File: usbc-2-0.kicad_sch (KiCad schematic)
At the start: 7 parts

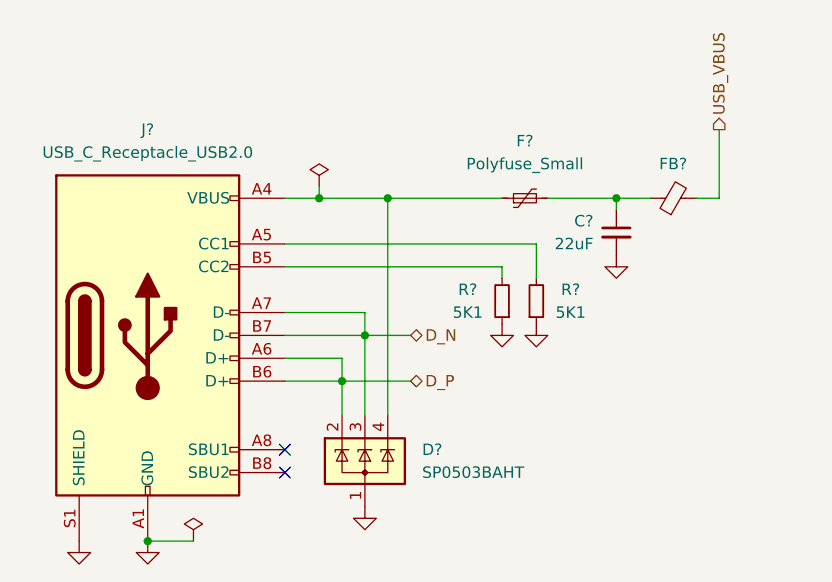
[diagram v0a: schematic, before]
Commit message: updated caps and power regulator
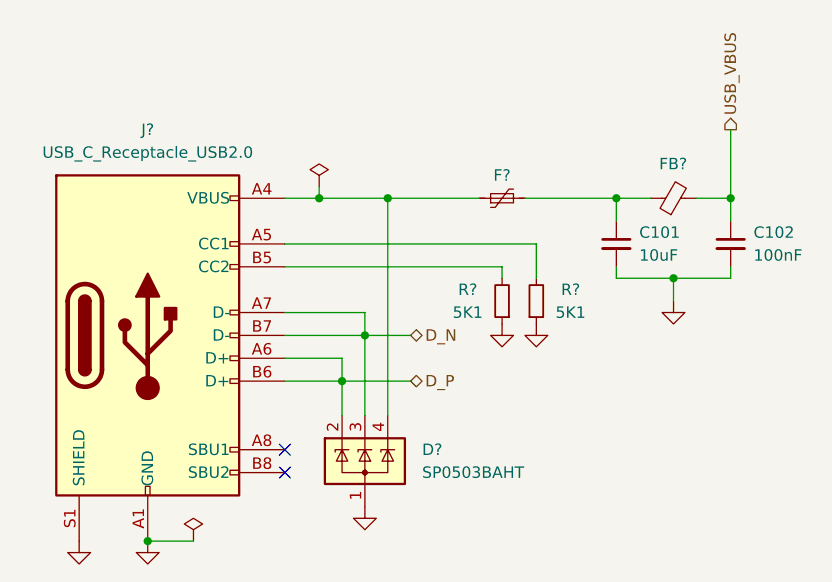
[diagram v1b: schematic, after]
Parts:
- removed C?: 22uF, Capacitor_SMD:C_0805_2012Metric, symbol Device:C_Small
- added C101: 10uF, Capacitor_SMD:C_0805_2012Metric, symbol Device:C_Small
- added C102: 100nF, Capacitor_SMD:C_0603_1608Metric, symbol Device:C_Small
- D?: LCSC (none) -> C7074
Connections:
- net GND: now also C101.2, C102.2
- net USB_VBUS: now also C102.1
- net at F?.2, FB?.1: now also C101.1
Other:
- moved on the sheet: F?
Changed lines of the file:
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@@
 (kicad_sch (version 20230121) (generator eeschema)
   (paper "A5")
+  (junction (at 109.22 46.99) (diameter 0) (color 0 0 0 0)
+  )
   (junction (at 74.93 53.34) (diameter 0) (color 0 0 0 0)
   )
@@
   )
   (junction (at 77.47 38.1) (diameter 0) (color 0 0 0 0)
+  )
+  (junction (at 115.57 38.1) (diameter 0) (color 0 0 0 0)
   )
   (junction (at 50.8 76.2) (diameter 0) (color 0 0 0 0)
@@
     (stroke (width 0) (type default))
   )
-  (wire (pts (xy 114.3 30.48) (xy 114.3 38.1))
+  (wire (pts (xy 115.57 30.48) (xy 115.57 38.1))
     (stroke (width 0) (type default))
   )
@@
     (stroke (width 0) (type default))
   )
+  (wire (pts (xy 115.57 46.99) (xy 115.57 45.72))
+    (stroke (width 0) (type default))
+  )
+  (wire (pts (xy 109.22 46.99) (xy 115.57 46.99))
+    (stroke (width 0) (type default))
+  )
   (wire (pts (xy 74.93 53.34) (xy 74.93 62.23))
     (stroke (width 0) (type default))
   )
-  (wire (pts (xy 102.87 39.37) (xy 102.87 38.1))
+  (wire (pts (xy 102.87 40.64) (xy 102.87 38.1))
     (stroke (width 0) (type default))
   )
@@
     (stroke (width 0) (type default))
   )
+  (wire (pts (xy 109.22 46.99) (xy 102.87 46.99))
+    (stroke (width 0) (type default))
+  )
   (wire (pts (xy 74.93 50.8) (xy 74.93 53.34))
     (stroke (width 0) (type default))
@@
     (stroke (width 0) (type default))
   )
-  (wire (pts (xy 77.47 38.1) (xy 90.17 38.1))
-    (stroke (width 0) (type default))
-  )
-  (wire (pts (xy 114.3 38.1) (xy 111.76 38.1))
+  (wire (pts (xy 77.47 38.1) (xy 87.63 38.1))
+    (stroke (width 0) (type default))
+  )
+  (wire (pts (xy 115.57 38.1) (xy 111.76 38.1))
+    (stroke (width 0) (type default))
+  )
+  (wire (pts (xy 115.57 38.1) (xy 115.57 40.64))
     (stroke (width 0) (type default))
   )
@@
     (stroke (width 0) (type default))
   )
+  (wire (pts (xy 102.87 46.99) (xy 102.87 45.72))
+    (stroke (width 0) (type default))
+  )
   (wire (pts (xy 50.8 76.2) (xy 55.88 76.2))
     (stroke (width 0) (type default))
@@
     (stroke (width 0) (type default))
   )
+  (wire (pts (xy 109.22 49.53) (xy 109.22 46.99))
+    (stroke (width 0) (type default))
+  )
   (wire (pts (xy 66.04 45.72) (xy 90.17 45.72))
     (stroke (width 0) (type default))
   )
-  (wire (pts (xy 95.25 38.1) (xy 102.87 38.1))
+  (wire (pts (xy 92.71 38.1) (xy 102.87 38.1))
     (stroke (width 0) (type default))
   )
@@
     (effects (font (size 1.27 1.27)) (justify left))
   )
-  (hierarchical_label "USB_VBUS" (shape output) (at 114.3 30.48 90) (fields_autoplaced)
+  (hierarchical_label "USB_VBUS" (shape output) (at 115.57 30.48 90) (fields_autoplaced)
     (effects (font (size 1.27 1.27)) (justify left))
   )
@@
     )
     (property "Datasheet" "http://www.littelfuse.com/~/media/files/littelfuse/technical%20resources/documents/data%20sheets/sp05xxba.pdf" (at 78.105 64.135 0)
+      (effects (font (size 1.27 1.27)) hide)
+    )
+    (property "LCSC" "C7074" (at 74.93 67.31 0)
       (effects (font (size 1.27 1.27)) hide)
     )
@@
     )
   )
+  (symbol (lib_id "Device:C_Small") (at 115.57 43.18 0) (unit 1)
+    (in_bom yes) (on_board yes) (dnp no)
+    (property "Reference" "C102" (at 118.11 41.91 0)
+      (effects (font (size 1.27 1.27)) (justify left))
+    )
+    (property "Value" "100nF" (at 118.11 44.45 0)
+      (effects (font (size 1.27 1.27)) (justify left))
+    )
+    (property "Footprint" "Capacitor_SMD:C_0603_1608Metric" (at 115.57 43.18 0)
+      (effects (font (size 1.27 1.27)) hide)
+    )
+    (property "Datasheet" "~" (at 115.57 43.18 0)
+      (effects (font (size 1.27 1.27)) hide)
+    )
+    (property "LCSC" "C14663" (at 115.57 43.18 0)
+      (effects (font (size 1.27 1.27)) hide)
+    )
+    (pin "1")
+    (pin "2")
+    (instances
+      (project "arudino-clone"
+        (path "/7b2b1845-59f7-4bfa-9efc-3639d821cf70"
+          (reference "C102") (unit 1)
+        )
+        (path "/7b2b1845-59f7-4bfa-9efc-3639d821cf70/42f81444-0f87-48cc-869b-f9c5fa4e11c4"
+          (reference "C202") (unit 1)
+        )
+      )
+    )
+  )
   (symbol (lib_id "Device:FerriteBead_Small") (at 109.22 38.1 90) (unit 1)
     (in_bom yes) (on_board yes) (dnp no) (fields_autoplaced)
@@
     )
   )
-  (symbol (lib_id "Device:Polyfuse_Small") (at 92.71 38.1 90) (unit 1)
-    (in_bom yes) (on_board yes) (dnp no) (fields_autoplaced)
-    (property "Reference" "F?" (at 92.71 31.75 90)
-      (effects (font (size 1.27 1.27)))
-    )
-    (property "Value" "Polyfuse_Small" (at 92.71 34.29 90)
-      (effects (font (size 1.27 1.27)))
-    )
-    (property "Footprint" "Fuse:Fuse_0603_1608Metric" (at 97.79 36.83 0)
+  (symbol (lib_id "Device:C_Small") (at 102.87 43.18 0) (unit 1)
+    (in_bom yes) (on_board yes) (dnp no)
+    (property "Reference" "C101" (at 105.41 41.91 0)
+      (effects (font (size 1.27 1.27)) (justify left))
+    )
+    (property "Value" "10uF" (at 105.41 44.45 0)
+      (effects (font (size 1.27 1.27)) (justify left))
+    )
+    (property "Footprint" "Capacitor_SMD:C_0805_2012Metric" (at 102.87 43.18 0)
+      (effects (font (size 1.27 1.27)) hide)
+    )
+    (property "Datasheet" "~" (at 102.87 43.18 0)
+      (effects (font (size 1.27 1.27)) hide)
+    )
+    (property "LCSC" "C15850" (at 102.87 43.18 0)
+      (effects (font (size 1.27 1.27)) hide)
+    )
+    (pin "1")
+    (pin "2")
+    (instances
+      (project "arudino-clone"
+        (path "/7b2b1845-59f7-4bfa-9efc-3639d821cf70"
+          (reference "C101") (unit 1)
+        )
+        (path "/7b2b1845-59f7-4bfa-9efc-3639d821cf70/42f81444-0f87-48cc-869b-f9c5fa4e11c4"
+          (reference "C201") (unit 1)
+        )
+      )
+    )
+  )
+  (symbol (lib_id "Device:Polyfuse_Small") (at 90.17 38.1 90) (unit 1)
+    (in_bom yes) (on_board yes) (dnp no) (fields_autoplaced)
+    (property "Reference" "F?" (at 90.17 35.56 90)
+      (effects (font (size 1.27 1.27)))
+    )
+    (property "Value" "Polyfuse_Small" (at 90.17 34.29 90)
+      (effects (font (size 1.27 1.27)) hide)
+    )
+    (property "Footprint" "Fuse:Fuse_0603_1608Metric" (at 95.25 36.83 0)
       (effects (font (size 1.27 1.27)) (justify left) hide)
     )
-    (property "Datasheet" "~" (at 92.71 38.1 0)
-      (effects (font (size 1.27 1.27)) hide)
-    )
-    (property "LCSC" "C2757930" (at 92.71 38.1 0)
+    (property "Datasheet" "~" (at 90.17 38.1 0)
+      (effects (font (size 1.27 1.27)) hide)
+    )
+    (property "LCSC" "C2757930" (at 90.17 38.1 0)
       (effects (font (size 1.27 1.27)) hide)
     )
@@
     )
   )
-  (symbol (lib_id "Device:C_Small") (at 102.87 41.91 0) (mirror y) (unit 1)
-    (in_bom yes) (on_board yes) (dnp no)
-    (property "Reference" "C?" (at 100.33 40.64 0)
-      (effects (font (size 1.27 1.27)) (justify left))
-    )
-    (property "Value" "22uF" (at 100.33 43.18 0)
-      (effects (font (size 1.27 1.27)) (justify left))
-    )
-    (property "Footprint" "Capacitor_SMD:C_0805_2012Metric" (at 102.87 41.91 0)
-      (effects (font (size 1.27 1.27)) hide)
-    )
-    (property "Datasheet" "~" (at 102.87 41.91 0)
-      (effects (font (size 1.27 1.27)) hide)
-    )
-    (property "LCSC" "C45783" (at 102.87 41.91 0)
-      (effects (font (size 1.27 1.27)) hide)
-    )
-    (pin "1")
-    (pin "2")
-    (instances
-      (project "arudino-clone"
-        (path "/7b2b1845-59f7-4bfa-9efc-3639d821cf70"
-          (reference "C?") (unit 1)
-        )
-        (path "/7b2b1845-59f7-4bfa-9efc-3639d821cf70/42f81444-0f87-48cc-869b-f9c5fa4e11c4"
-          (reference "C201") (unit 1)
-        )
-      )
-    )
-  )
-  (symbol (lib_id "power:GND") (at 102.87 44.45 0) (unit 1)
-    (in_bom yes) (on_board yes) (dnp no) (fields_autoplaced)
-    (property "Reference" "#PWR?" (at 102.87 50.8 0)
-      (effects (font (size 1.27 1.27)) hide)
-    )
-    (property "Value" "GND" (at 102.87 49.53 0)
-      (effects (font (size 1.27 1.27)) hide)
-    )
-    (property "Footprint" "" (at 102.87 44.45 0)
-      (effects (font (size 1.27 1.27)) hide)
-    )
-    (property "Datasheet" "" (at 102.87 44.45 0)
-      (effects (font (size 1.27 1.27)) hide)
-    )
+  (symbol (lib_id "power:GND") (at 109.22 49.53 0) (unit 1)
+    (in_bom yes) (on_board yes) (dnp no) (fields_autoplaced)
+    (property "Reference" "#PWR?" (at 109.22 55.88 0)
+      (effects (font (size 1.27 1.27)) hide)
+    )
+    (property "Value" "GND" (at 109.22 54.61 0)
+      (effects (font (size 1.27 1.27)) hide)
+    )
+    (property "Footprint" "" (at 109.22 49.53 0)
+      (effects (font (size 1.27 1.27)) hide)
+    )
+    (property "Datasheet" "" (at 109.22 49.53 0)
+      (effects (font (size 1.27 1.27)) hide)
+    )
